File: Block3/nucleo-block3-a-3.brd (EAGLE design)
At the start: 100.3 x 80 mm, 51 parts, among them J4 MODJACK6P6C-MJ3245-66-0CONN_M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, J5 MODJACK6P6C-MJ3245-66-0CONN_M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, Q1 NPN-23, Q2 BSS84, U1 TC4428ACOA, U2 TC4428ACOA, U3 TC4428ACOA

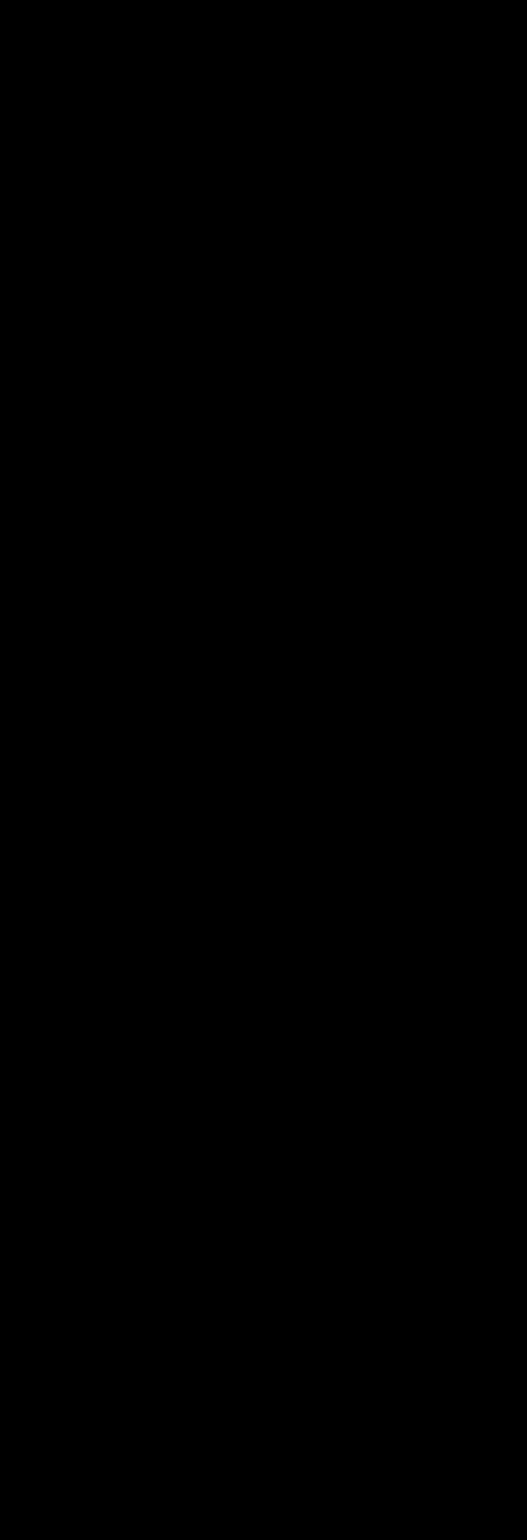
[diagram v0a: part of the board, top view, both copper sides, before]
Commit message: Adds loconet interrupt circuit. Links more things to the nucleo.
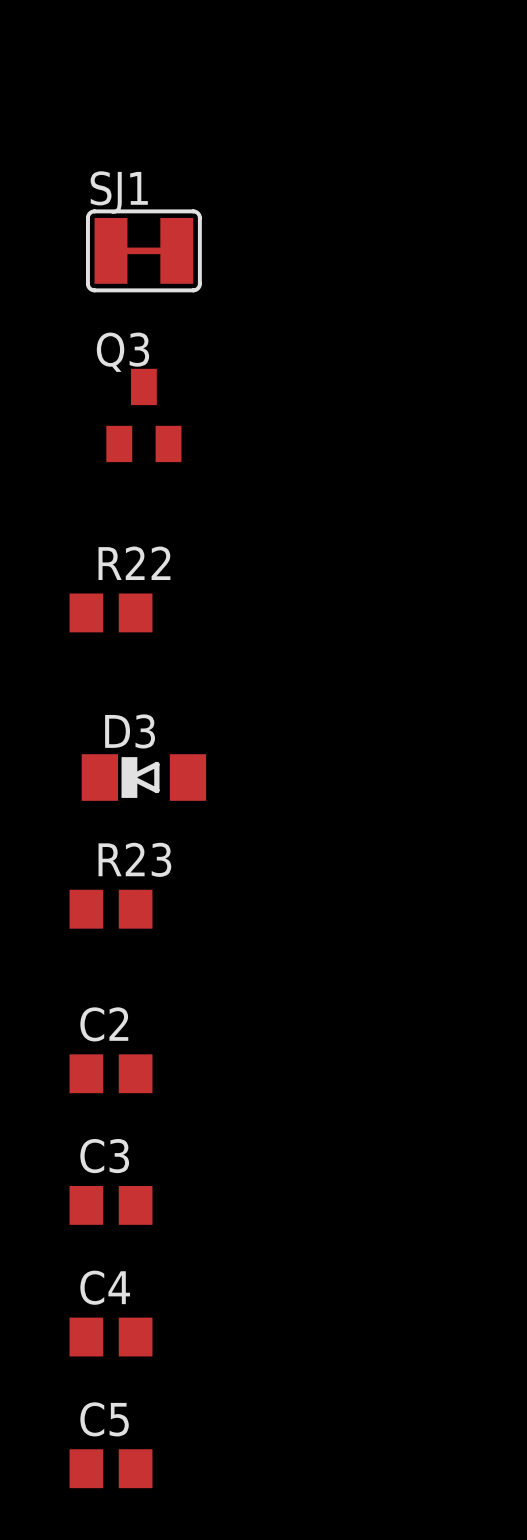
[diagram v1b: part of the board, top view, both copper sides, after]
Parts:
- added C2, C3, C4: (no value), rcl:C0805
- added C5: 2.2nF, rcl:C0805
- added D3: (no value), diode:MINIMELF
- added Q3: BSS84, eagleparts:SOT23-PCH
- added R22: 1M, rcl:R0805
- added R23: 10k, rcl:R0805
- added SJ1: (no value), eagleparts:SJW-C
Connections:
- removed net N$9: Q1.3, R5.1, R6.2
- new net LN-INT: G1.PC4, Q3.3
- new net LN-RX-S: D3.C, Q1.3, R5.1, R6.2
- new net LN-TX-P: G1.PC5, Q2.3, R7.1
- new net N$20: G1.PB14, SJ1.2
- new net N$22: C5.1, Q3.1, R22.2, R23.2
- net +5V: now also C2.2, C3.2, C4.2
- net GND: now also C2.1, C3.1, C4.1
- net LN-RX: now also G1.PA10, SJ1.1
- net LN-TX: now also C5.2, G1.PA9, Q3.2, R22.1
- net N$10: now also D3.A, R23.1; no longer Q2.3, R7.1
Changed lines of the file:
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@@
 <attribute name="VALUE" x="-99.5188" y="-315.595" size="1.27" layer="27" ratio="6"/>
+</element>
+<element name="SJ1" library="eagleparts" package="SJW-C" value="" x="-110.49" y="-335.28" smashed="yes">
+<attribute name="NAME" x="-112.649" y="-333.502" size="1.27" layer="25" ratio="10"/>
+<attribute name="VALUE" x="-109.49" y="-335.28" size="0.02" layer="27"/>
+</element>
+<element name="Q3" library="eagleparts" package="SOT23-PCH" value="BSS84" x="-110.49" y="-341.63" smashed="yes">
+<attribute name="NAME" x="-112.395" y="-339.725" size="1.27" layer="25"/>
+<attribute name="POPULARITY" value="21" x="-110.49" y="-341.63" size="1.778" layer="27" display="off"/>
+<attribute name="VALUE" x="-112.395" y="-344.805" size="1.27" layer="27"/>
+</element>
+<element name="R22" library="rcl" library_urn="urn:adsk.eagle:library:334" package="R0805" package3d_urn="urn:adsk.eagle:package:23553/2" value="1M" x="-111.76" y="-349.25" smashed="yes">
+<attribute name="NAME" x="-112.395" y="-347.98" size="1.27" layer="25"/>
+<attribute name="POPULARITY" value="86" x="-111.76" y="-349.25" size="1.778" layer="27" display="off"/>
+<attribute name="SPICEPREFIX" value="R" x="-111.76" y="-349.25" size="1.778" layer="27" display="off"/>
+<attribute name="VALUE" x="-112.395" y="-351.79" size="1.27" layer="27"/>
+</element>
+<element name="D3" library="diode" library_urn="urn:adsk.eagle:library:210" package="MINIMELF" package3d_urn="urn:adsk.eagle:package:43429/2" value="" x="-110.49" y="-355.6" smashed="yes">
+<attribute name="NAME" x="-112.141" y="-354.457" size="1.27" layer="25"/>
+<attribute name="POPULARITY" value="25" x="-110.49" y="-355.6" size="1.778" layer="27" display="off"/>
+<attribute name="VALUE" x="-112.141" y="-358.013" size="1.27" layer="27"/>
+</element>
+<element name="R23" library="rcl" library_urn="urn:adsk.eagle:library:334" package="R0805" package3d_urn="urn:adsk.eagle:package:23553/2" value="10k" x="-111.76" y="-360.68" smashed="yes">
+<attribute name="NAME" x="-112.395" y="-359.41" size="1.27" layer="25"/>
+<attribute name="POPULARITY" value="86" x="-111.76" y="-360.68" size="1.778" layer="27" display="off"/>
+<attribute name="SPICEPREFIX" value="R" x="-111.76" y="-360.68" size="1.778" layer="27" display="off"/>
+<attribute name="VALUE" x="-112.395" y="-363.22" size="1.27" layer="27"/>
+</element>
+<element name="C2" library="rcl" library_urn="urn:adsk.eagle:library:334" package="C0805" package3d_urn="urn:adsk.eagle:package:23617/2" value="" x="-111.76" y="-367.03" smashed="yes">
+<attribute name="NAME" x="-113.03" y="-365.76" size="1.27" layer="25"/>
+<attribute name="POPULARITY" value="88" x="-111.76" y="-367.03" size="1.778" layer="27" display="off"/>
+<attribute name="SPICEPREFIX" value="C" x="-111.76" y="-367.03" size="1.778" layer="27" display="off"/>
+<attribute name="VALUE" x="-113.03" y="-369.57" size="1.27" layer="27"/>
+</element>
+<element name="C3" library="rcl" library_urn="urn:adsk.eagle:library:334" package="C0805" package3d_urn="urn:adsk.eagle:package:23617/2" value="" x="-111.76" y="-372.11" smashed="yes">
+<attribute name="NAME" x="-113.03" y="-370.84" size="1.27" layer="25"/>
+<attribute name="POPULARITY" value="88" x="-111.76" y="-372.11" size="1.778" layer="27" display="off"/>
+<attribute name="SPICEPREFIX" value="C" x="-111.76" y="-372.11" size="1.778" layer="27" display="off"/>
+<attribute name="VALUE" x="-113.03" y="-374.65" size="1.27" layer="27"/>
+</element>
+<element name="C4" library="rcl" library_urn="urn:adsk.eagle:library:334" package="C0805" package3d_urn="urn:adsk.eagle:package:23617/2" value="" x="-111.76" y="-377.19" smashed="yes">
+<attribute name="NAME" x="-113.03" y="-375.92" size="1.27" layer="25"/>
+<attribute name="POPULARITY" value="88" x="-111.76" y="-377.19" size="1.778" layer="27" display="off"/>
+<attribute name="SPICEPREFIX" value="C" x="-111.76" y="-377.19" size="1.778" layer="27" display="off"/>
+<attribute name="VALUE" x="-113.03" y="-379.73" size="1.27" layer="27"/>
+</element>
+<element name="C5" library="rcl" library_urn="urn:adsk.eagle:library:334" package="C0805" package3d_urn="urn:adsk.eagle:package:23617/2" value="2.2nF" x="-111.76" y="-382.27" smashed="yes">
+<attribute name="NAME" x="-113.03" y="-381" size="1.27" layer="25"/>
+<attribute name="POPULARITY" value="88" x="-111.76" y="-382.27" size="1.778" layer="27" display="off"/>
+<attribute name="SPICEPREFIX" value="C" x="-111.76" y="-382.27" size="1.778" layer="27" display="off"/>
+<attribute name="VALUE" x="-113.03" y="-384.81" size="1.27" layer="27"/>
 </element>
 </elements>
@@
 <contactref element="LED8" pad="3"/>
 <contactref element="LED9" pad="3"/>
+<contactref element="C2" pad="1"/>
+<contactref element="C4" pad="1"/>
+<contactref element="C3" pad="1"/>
 <wire x1="-103.19" y1="-120.48" x2="-103.19" y2="-148.59" width="0" layer="19" extent="1-1"/>
 <wire x1="-103.19" y1="-114.3" x2="-103.19" y2="-120.48" width="0" layer="19" extent="1-1"/>
@@
 <wire x1="-66.0908" y1="-244.22" x2="-66.0908" y2="-268.35" width="0" layer="19" extent="1-1"/>
 <wire x1="-66.0908" y1="-220.09" x2="-66.0908" y2="-244.22" width="0" layer="19" extent="1-1"/>
+<wire x1="-112.71" y1="-367.03" x2="-95.3008" y2="-316.61" width="0" layer="19" extent="1-1"/>
+<wire x1="-112.71" y1="-372.11" x2="-112.71" y2="-367.03" width="0" layer="19" extent="1-1"/>
+<wire x1="-112.71" y1="-377.19" x2="-112.71" y2="-372.11" width="0" layer="19" extent="1-1"/>
 <wire x1="-24.455" y1="-67.635" x2="-103.19" y2="-114.3" width="0" layer="19" extent="1-1"/>
 <wire x1="-20.35" y1="-74.19" x2="-24.455" y2="-67.635" width="0" layer="19" extent="1-1"/>
@@
 <contactref element="LED8" pad="1"/>
 <contactref element="LED9" pad="1"/>
+<contactref element="C2" pad="2"/>
+<contactref element="C4" pad="2"/>
+<contactref element="C3" pad="2"/>
+<wire x1="-110.81" y1="-372.11" x2="-110.81" y2="-377.19" width="0" layer="19" extent="1-1"/>
+<wire x1="-110.81" y1="-367.03" x2="-110.81" y2="-372.11" width="0" layer="19" extent="1-1"/>
+<wire x1="-100.2792" y1="-313.31" x2="-110.81" y2="-367.03" width="0" layer="19" extent="1-1"/>
 <wire x1="-100.2792" y1="-289.18" x2="-100.2792" y2="-313.31" width="0" layer="19" extent="1-1"/>
 <wire x1="-100.2792" y1="-265.05" x2="-100.2792" y2="-289.18" width="0" layer="19" extent="1-1"/>
@@
 <contactref element="Q2" pad="1"/>
 <contactref element="R10" pad="1"/>
+<contactref element="G1" pad="PA9"/>
+<contactref element="Q3" pad="2"/>
+<contactref element="R22" pad="1"/>
+<contactref element="C5" pad="2"/>
 <wire x1="-105.09" y1="-154.94" x2="-105.09" y2="-135.72" width="0" layer="19" extent="1-1"/>
+<wire x1="-109.54" y1="-342.73" x2="-105.09" y2="-154.94" width="0" layer="19" extent="1-1"/>
+<wire x1="-112.71" y1="-349.25" x2="-109.54" y2="-342.73" width="0" layer="19" extent="1-1"/>
+<wire x1="-110.81" y1="-382.27" x2="-112.71" y2="-349.25" width="0" layer="19" extent="1-1"/>
+<wire x1="78.74" y1="46.99" x2="-105.09" y2="-135.72" width="0" layer="19" extent="1-1"/>
 </signal>
 <signal name="VCC">
@@
 <wire x1="17.78" y1="67.31" x2="-103.19" y2="-135.72" width="0" layer="19" extent="1-1"/>
 </signal>
-<signal name="N$10">
+<signal name="LN-TX-P">
 <contactref element="Q2" pad="3"/>
 <contactref element="R7" pad="1"/>
+<contactref element="G1" pad="PC5"/>
 <wire x1="-104.14" y1="-133.52" x2="-105.09" y2="-142.24" width="0" layer="19" extent="1-1"/>
+<wire x1="81.28" y1="67.31" x2="-104.14" y2="-133.52" width="0" layer="19" extent="1-1"/>
 </signal>
 <signal name="N$11">
@@
 <wire x1="-105.09" y1="-120.48" x2="-103.19" y2="-142.24" width="0" layer="19" extent="1-1"/>
 </signal>
-<signal name="N$9">
+<signal name="LN-RX-S">
 <contactref element="R5" pad="1"/>
 <contactref element="R6" pad="2"/>
 <contactref element="Q1" pad="3"/>
+<contactref element="D3" pad="C"/>
 <wire x1="-104.14" y1="-118.28" x2="-103.19" y2="-127" width="0" layer="19" extent="1-1"/>
 <wire x1="-105.09" y1="-107.95" x2="-104.14" y2="-118.28" width="0" layer="19" extent="1-1"/>
+<wire x1="-112.19" y1="-355.6" x2="-103.19" y2="-127" width="0" layer="19" extent="1-1"/>
 </signal>
 <signal name="LN-RX">
 <contactref element="R6" pad="1"/>
+<contactref element="SJ1" pad="1"/>
+<contactref element="G1" pad="PA10"/>
+<wire x1="-111.76" y1="-335.28" x2="-105.09" y2="-127" width="0" layer="19" extent="1-1"/>
+<wire x1="78.74" y1="31.75" x2="-105.09" y2="-127" width="0" layer="19" extent="1-1"/>
 </signal>
 <signal name="N$8">
@@
 <wire x1="-71.0692" y1="-292.48" x2="-95.3008" y2="-313.31" width="0" layer="19" extent="1-1"/>
 </signal>
+<signal name="N$20">
+<contactref element="G1" pad="PB14"/>
+<contactref element="SJ1" pad="2"/>
+<wire x1="81.28" y1="39.37" x2="-109.22" y2="-335.28" width="0" layer="19" extent="1-1"/>
+</signal>
+<signal name="N$10">
+<contactref element="D3" pad="A"/>
+<contactref element="R23" pad="1"/>
+<wire x1="-108.79" y1="-355.6" x2="-112.71" y2="-360.68" width="0" layer="19" extent="1-1"/>
+</signal>
+<signal name="N$22">
+<contactref element="C5" pad="1"/>
+<contactref element="R22" pad="2"/>
+<contactref element="Q3" pad="1"/>
+<contactref element="R23" pad="2"/>
+<wire x1="-110.81" y1="-360.68" x2="-112.71" y2="-382.27" width="0" layer="19" extent="1-1"/>
+<wire x1="-110.81" y1="-349.25" x2="-110.81" y2="-360.68" width="0" layer="19" extent="1-1"/>
+<wire x1="-111.44" y1="-342.73" x2="-110.81" y2="-349.25" width="0" layer="19" extent="1-1"/>
+</signal>
+<signal name="LN-INT">
+<contactref element="Q3" pad="3"/>
+<contactref element="G1" pad="PC4"/>
+<wire x1="81.28" y1="31.75" x2="-110.49" y2="-340.53" width="0" layer="19" extent="1-1"/>
+</signal>
 </signals>

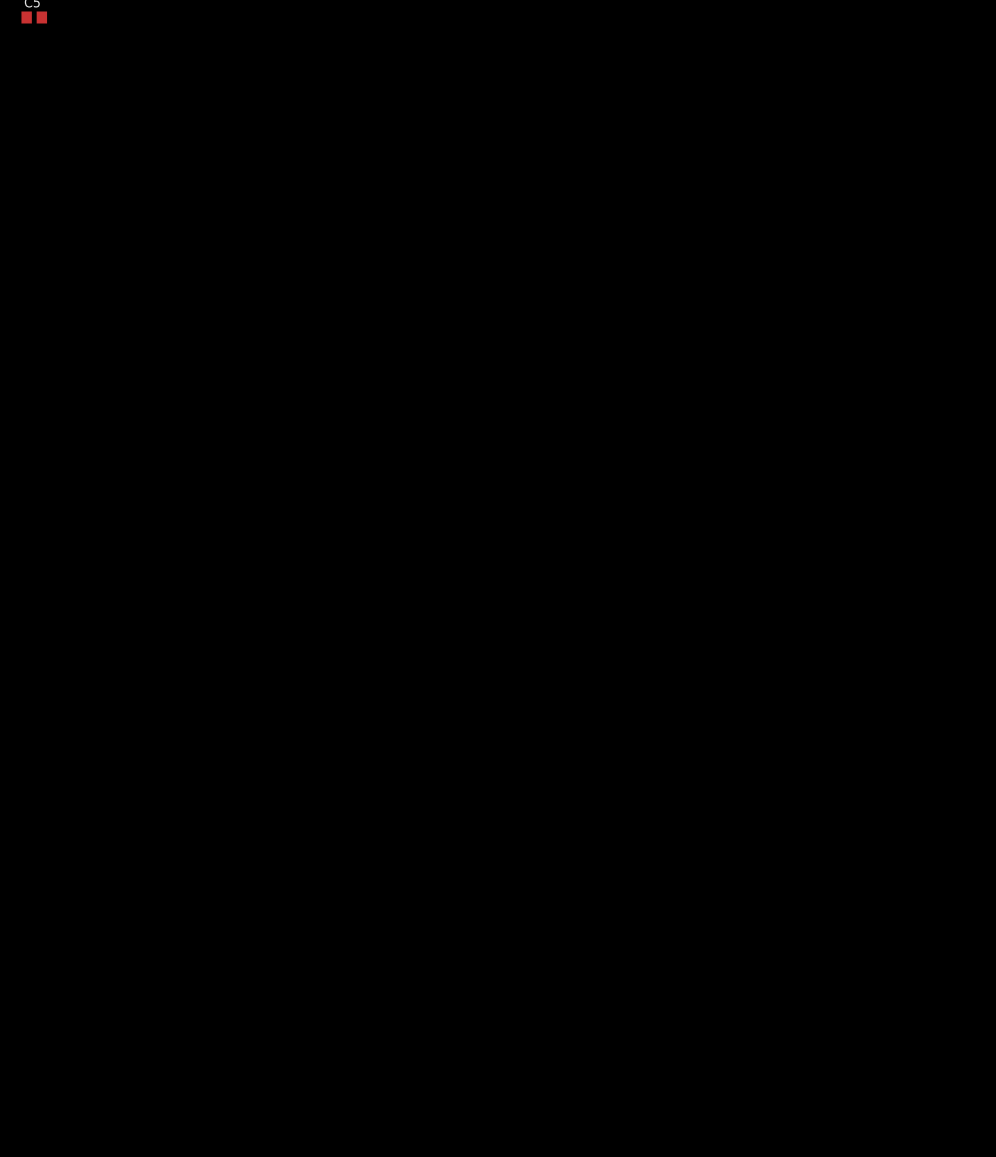
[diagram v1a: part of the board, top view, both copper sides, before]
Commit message: Adds analog read-in buttons.
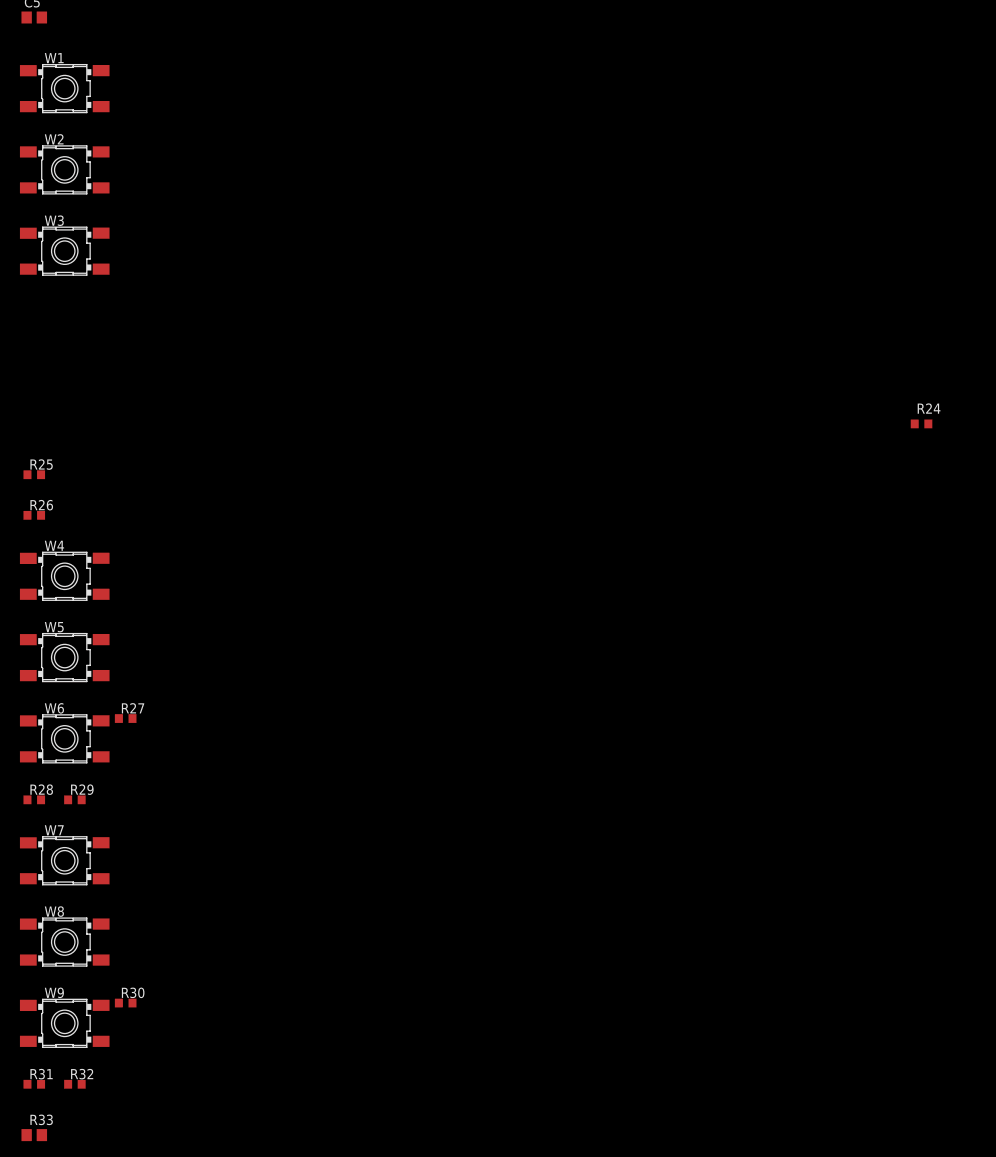
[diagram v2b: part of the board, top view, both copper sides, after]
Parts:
- added R24: 10k, rcl:R0603
- added R25: 3k3, rcl:R0603
- added R26: 2k2, rcl:R0603
- added R27: 1k5, rcl:R0603
- added R28, R29, R30, R31, R32: 47k, rcl:R0603
- added R33: 1k, rcl:R0805
- added W1, W2, W3, W4, W5, W6, W7, W8, W9: W1, g-e2e-training:TACTSW-6X6
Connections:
- new net BTNADC: G1.PB0, R24.1, R25.1, R26.1, R27.1, R28.1, R29.1, R30.1, R31.1, R32.1, R33.2
- new net N$21: R25.2, W2.4
- new net N$23: R26.2, W3.4
- new net N$24: W1.1, W1.2, W2.1, W2.2, W3.1, W3.2
- new net N$26: R27.2, W4.4
- new net N$27: R28.2, W5.4
- new net N$28: R29.2, W6.4
- new net N$29: W4.1, W4.2, W5.1, W5.2, W6.1, W6.2
- new net N$32: R30.2, W7.4
- new net N$33: R31.2, W8.4
- new net N$34: R32.2, W9.4
- new net N$36: W7.1, W7.2, W8.1, W8.2, W9.1, W9.2
- new net N$9: R24.2, W1.4
- net VCC: now also R33.1

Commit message: Adds routing of the loconet input voltage to an NC pin to drive the 5V switcher. Adds a comparator based loconet input voltage decoder. Finishes the button grid.
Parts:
- added C6, C7: (no value), rcl:C0805
- added IC1: TL331, linear:DBV-R-PDSO-G5
- added R34: 1k, rcl:R0805
- added R35: 4k7, rcl:R0805
- added R36, R38, R39: 47k, rcl:R0805
- added R37: 10k, rcl:R0805
- JP1: device jumper:JP1 -> jumper:JP2Q
- R24: value 10k -> 8k2
- R26: value 2k2 -> 2k
- R27: value 1k5 -> 1200
- R28: value 47k -> 820
- R29: value 47k -> 510
- R30: value 47k -> 330
- R31: value 47k -> 200
- R32: value 47k -> 100
- moved JP1 326.5 mm to (-119.4, -519.4)
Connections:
- removed net N$29: W4.1, W4.2, W5.1, W5.2, W6.1, W6.2
- removed net N$36: W7.1, W7.2, W8.1, W8.2, W9.1, W9.2
- new net +15V: G1.NC4, JP1.1
- new net LNPLUS: C7.2, D1.C, D2.C, IC1.5, JP1.2, JP1.4
- new net N$25: IC1.4, R37.2, R38.1, R39.1
- net +12V: now also JP1.3; no longer JP1.2
- net +5V: now also R34.1, R37.1
- net GND: now also C6.1, C7.1, IC1.2, R35.2, W1.1, W1.2, W2.1, W2.2, W3.1, W3.2, W4.1, W4.2, W5.1, W5.2, W6.1, W6.2, W7.1, W7.2, W8.1, W8.2, W9.1, W9.2
- net LN-RX: now also R39.2
- net LN-RX-S: now also R36.1
- net N$24: now also C6.2, IC1.3, R36.2, R38.2; no longer W1.1, W1.2, W2.1, W2.2, W3.1, W3.2
- net N$8: now also IC1.1, R34.2, R35.1; no longer D1.C, D2.C, JP1.1
